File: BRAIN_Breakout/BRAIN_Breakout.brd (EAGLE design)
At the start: 160 x 100 mm, 101 parts

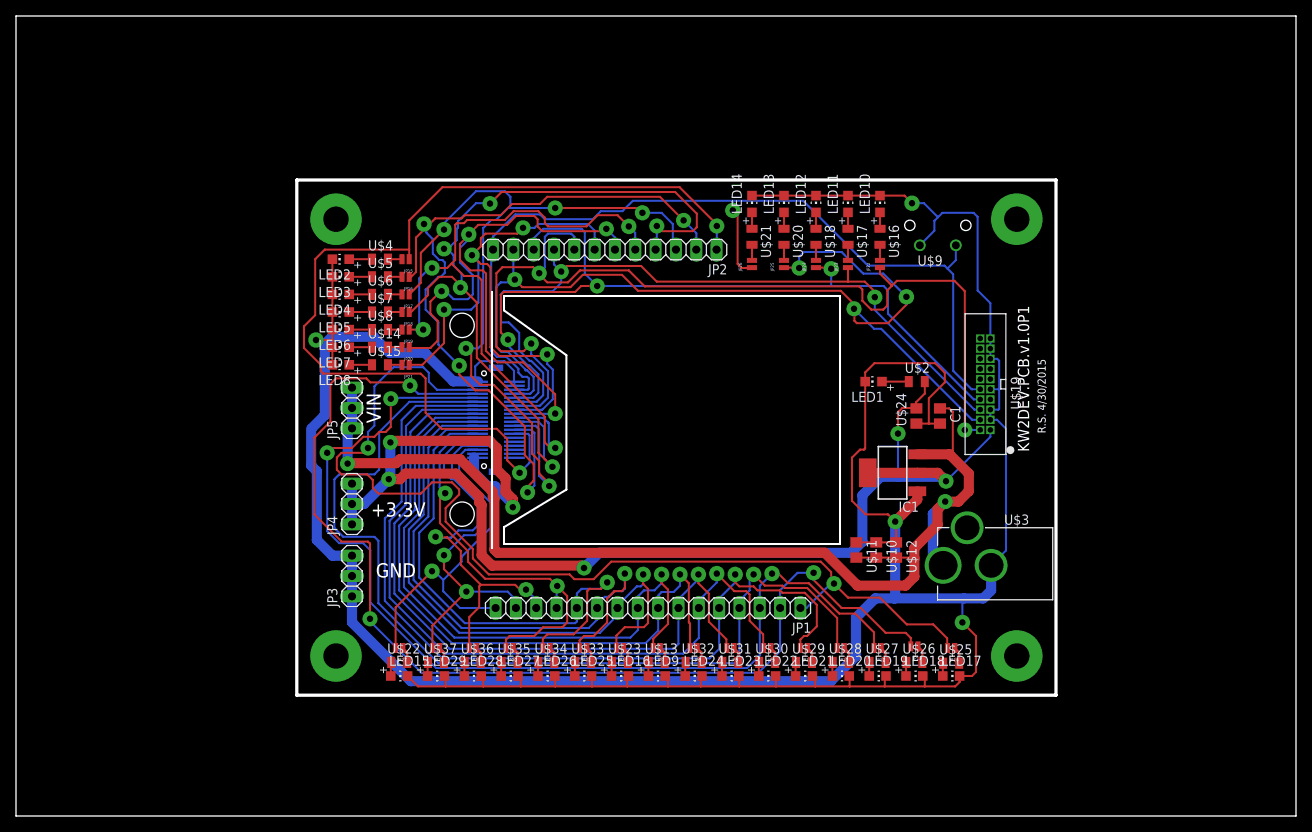
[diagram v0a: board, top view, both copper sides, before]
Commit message: Updated BRAIN Breakout with silkscreen
Added silkscreen fixes for production run
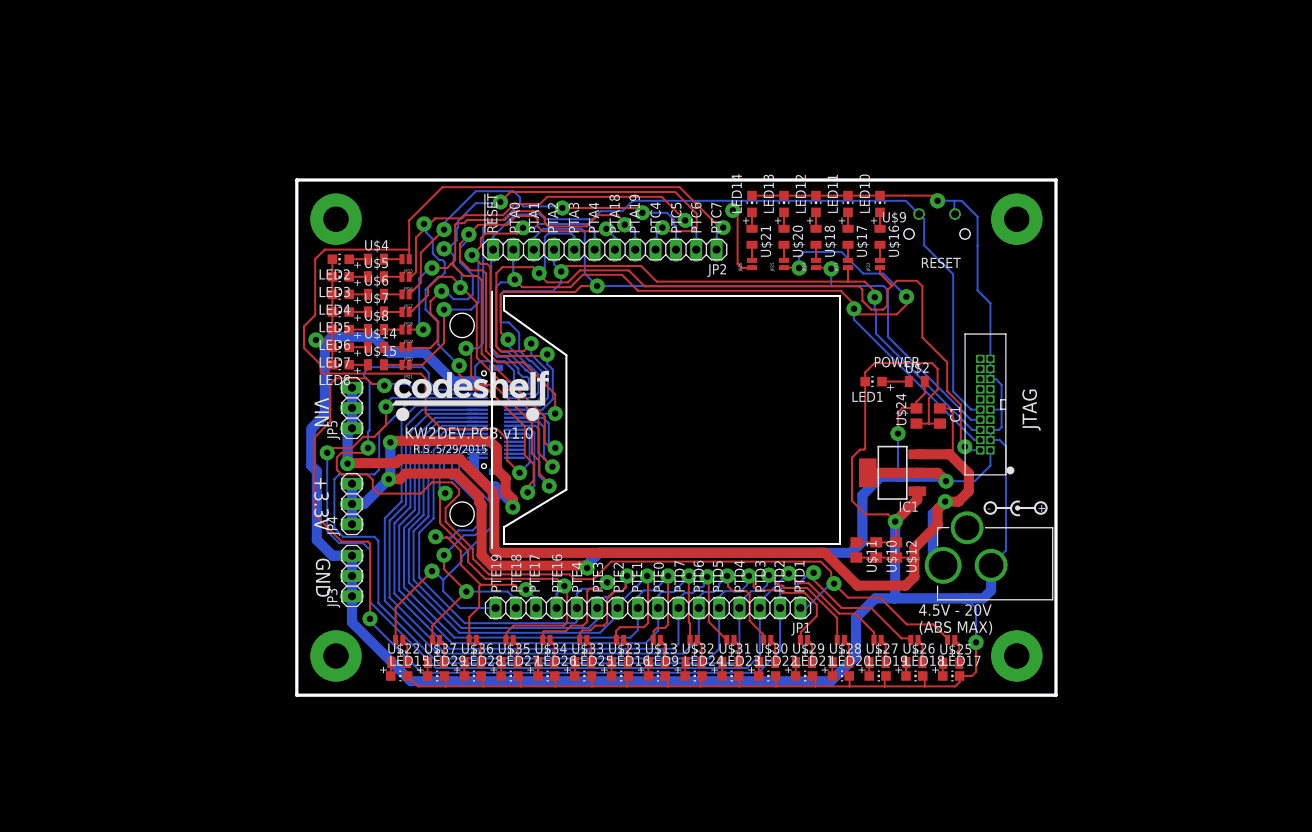
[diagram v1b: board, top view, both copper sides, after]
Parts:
- moved U$9 3.90 mm to (115.1, 75.2), turned to 180 degrees
- moved U$19 2.54 mm to (120.5, 52.1)
- moved JP10 1.00 mm to (98.5, 22.0)
- moved JP11 1.00 mm to (103.1, 22.0)
- moved JP12 1.00 mm to (107.7, 22.0)
- moved JP14 1.00 mm to (116.9, 22.0)
- moved JP27 1.00 mm to (47.9, 22.0)
- moved JP28 1.00 mm to (52.5, 22.0)
- moved JP29 1.00 mm to (57.1, 22.0)
- moved JP30 1.00 mm to (61.7, 22.0)
- moved JP31 1.00 mm to (66.3, 22.0)
- moved JP32 1.00 mm to (70.9, 22.0)
- moved JP33 1.00 mm to (75.5, 22.0)
- moved JP6 1.00 mm to (84.7, 22.0)
- moved JP7 1.00 mm to (80.1, 22.0)
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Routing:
- net GND: track 433.4 -> 430.0 mm
- net N$54: track 105.5 -> 108.2 mm
- net N$51: track 95.3 -> 98.0 mm
- net PTD3: track 127.7 -> 125.1 mm
- net PTD5: track 108.0 -> 106.4 mm
- net PTE0: track 83.3 -> 81.9 mm
- net PTD4: track 121.1 -> 119.7 mm
- net PTD1: track 131.0 -> 132.4 mm
- net N$23: track 101.6 -> 102.9 mm
- net PTE2: track 74.7 -> 73.4 mm
- net PTE19: track 44.7 -> 43.7 mm
- net PTE18: track 42.9 -> 41.9 mm
- net PTE17: track 47.9 -> 46.9 mm
- net N$70: track 2.03 -> 3.03 mm
- net N$69: track 2.03 -> 3.03 mm
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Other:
- board size 160 x 100 mm -> 94.9 x 64.4 mm
- board text added: "!RESET"
- board text added: "+"
- board text added: "-"
- board text added: "4.5V - 20V (ABS MAX)"
- board text added: "JTAG"
- board text added: "KW2DEV.PCB.v1.0"
- board text added: "POWER"
- board text added: "PTA0"
- board text added: "PTA1"
- board text added: "PTA18"
- board text added: "PTA19"
- board text added: "PTA2"
- board text added: "PTA3"
- board text added: "PTA4"
- board text added: "PTC4"
- board text added: "PTC5"
- board text added: "PTC6"
- board text added: "PTC7"
- board text added: "PTD1"
- board text added: "PTD2"
- board text added: "PTD3"
- board text added: "PTD4"
- board text added: "PTD5"
- board text added: "PTD6"
- board text added: "PTD7"
- board text added: "PTE0"
- board text added: "PTE1"
- board text added: "PTE16"
- board text added: "PTE17"
- board text added: "PTE18"
- board text added: "PTE19"
- board text added: "PTE2"
- board text added: "PTE3"
- board text added: "PTE4"
- board text added: "R.S. 5/29/2015"
- board text added: "RESET"
- board text removed: "KW2DEV.PCB.v1.0P1"
- board text removed: "R.S. 4/30/2015"

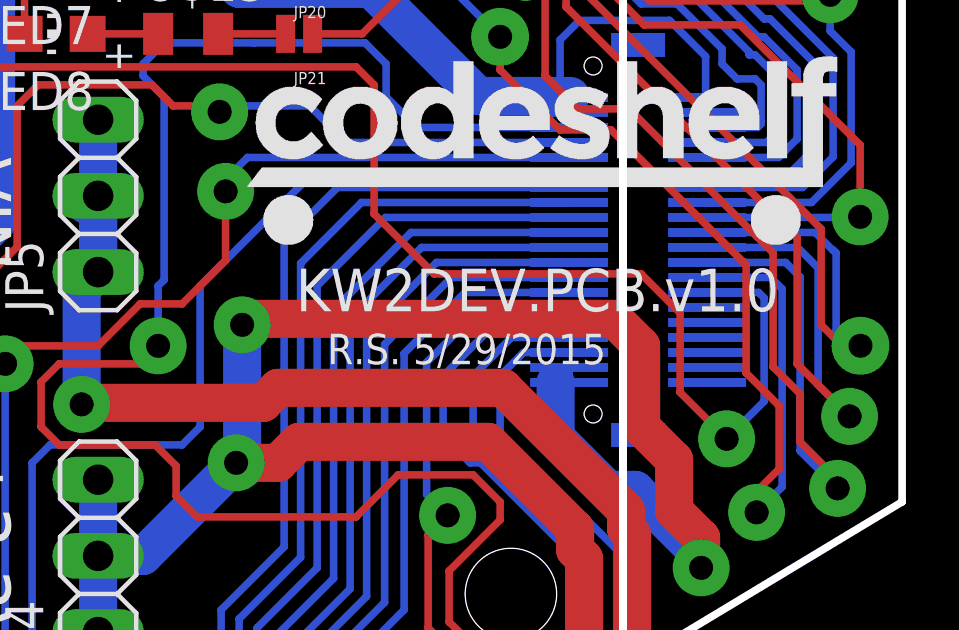
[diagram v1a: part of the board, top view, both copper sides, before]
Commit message: Commit board w/switches & fixes (updated to v1.1)
Hadn't previousy committed produced board (includes Gerbers). Just fixed
JTAG and RESET button ground traces and incremented date + version to
1.1 and 7/16
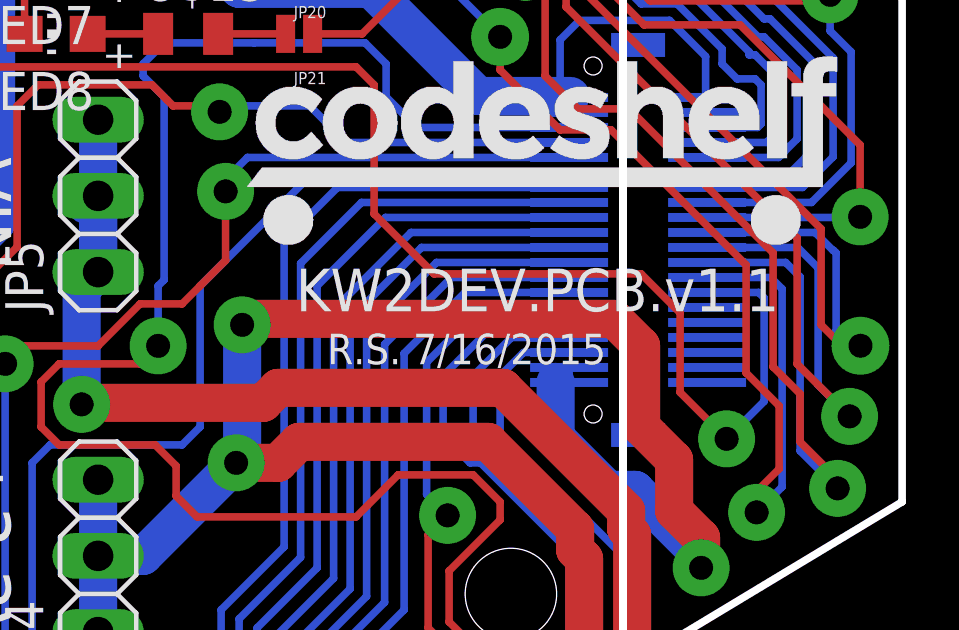
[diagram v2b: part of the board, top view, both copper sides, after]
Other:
- board text added: "KW2DEV.PCB.v1.1"
- board text added: "R.S. 7/16/2015"
- board text removed: "KW2DEV.PCB.v1.0"
- board text removed: "R.S. 5/29/2015"
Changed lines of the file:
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@@
 <?xml version="1.0" encoding="utf-8"?>
 <!DOCTYPE eagle SYSTEM "eagle.dtd">
-<eagle version="6.5.0">
+<eagle version="6.6.0">
 <drawing>
 <settings>
@@
 <text x="37.5" y="32.3" size="1.778" layer="21" font="vector" ratio="12" rot="SR270">GND</text>
 <text x="37.3" y="42.5" size="1.778" layer="21" font="vector" ratio="12" rot="SR270">+3.3V</text>
-<text x="64.7" y="48.5746" size="1.4224" layer="21" font="vector" ratio="15" rot="R180">KW2DEV.PCB.v1.0</text>
+<text x="64.7" y="48.5746" size="1.4224" layer="21" font="vector" ratio="15" rot="R180">KW2DEV.PCB.v1.1</text>
 <text x="60.6746" y="27.9" size="1.27" layer="21" font="vector" ratio="12" rot="R90">PTE19</text>
-<text x="49.63481875" y="45.387759375" size="1.016" layer="21" font="vector" ratio="15" rot="SR0">R.S. 5/29/2015</text>
+<text x="49.63481875" y="45.387759375" size="1.016" layer="21" font="vector" ratio="15" rot="SR0">R.S. 7/16/2015</text>
 <text x="63.1746" y="27.9" size="1.27" layer="21" font="vector" ratio="12" rot="R90">PTE18</text>
 <text x="65.4746" y="27.9" size="1.27" layer="21" font="vector" ratio="12" rot="R90">PTE17</text>
@@
 <element name="U$9" library="KW2" package="RA_BUTTON" value="RA_BUTTON" x="115.13" y="75.24" smashed="yes" rot="R180">
 <attribute name="NAME" x="111.37" y="75.48" size="1.27" layer="21" rot="R180"/>
+<attribute name="MFGN" value="TE" x="115.13" y="75.24" size="1.778" layer="27" rot="R180" display="off"/>
+<attribute name="MFGP" value="1825027-5" x="115.13" y="75.24" size="1.778" layer="27" rot="R180" display="off"/>
 </element>
 <element name="JP3" library="pinhead" package="1X03" value="" x="42" y="30" rot="R90"/>
@@
 <element name="U$21" library="GW-devices" package="RF-C0805" value="" x="92" y="72.4" rot="R270"/>
 <element name="JP26" library="SparkFun" package="SJ_2S-NO-NS" value="" x="92" y="69" rot="R90"/>
-<element name="LED15" library="adafruit" package="CHIP-LED0805" value="" x="47.9" y="17.5" rot="R270"/>
+<element name="LED15" library="adafruit" package="CHIP-LED0805" value="" x="47.9" y="17.5" rot="R270">
+<attribute name="MFGN" value="Kingbright" x="47.9" y="17.5" size="1.778" layer="27" rot="R270" display="off"/>
+</element>
 <element name="U$22" library="GW-devices" package="RF-C0805" value="" x="47.9" y="19.2"/>
 <element name="LED16" library="adafruit" package="CHIP-LED0805" value="" x="75.5" y="17.5" rot="R270"/>
@@
 <element name="LED27" library="adafruit" package="CHIP-LED0805" value="" x="61.7" y="17.5" rot="R270"/>
 <element name="U$35" library="GW-devices" package="RF-C0805" value="" x="61.7" y="19.2"/>
-<element name="LED28" library="adafruit" package="CHIP-LED0805" value="" x="57.1" y="17.5" rot="R270"/>
+<element name="LED28" library="adafruit" package="CHIP-LED0805" value="" x="57.1" y="17.5" rot="R270">
+<attribute name="MFGN" value="Kingbright" x="57.1" y="17.5" size="1.778" layer="27" rot="R270" display="off"/>
+</element>
 <element name="U$36" library="GW-devices" package="RF-C0805" value="" x="57.1" y="19.2"/>
 <element name="LED29" library="adafruit" package="CHIP-LED0805" value="" x="52.5" y="17.5" rot="R270"/>
